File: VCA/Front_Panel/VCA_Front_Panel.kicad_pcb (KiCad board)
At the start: 2 copper layers, 30 x 128.5 mm, 3 parts

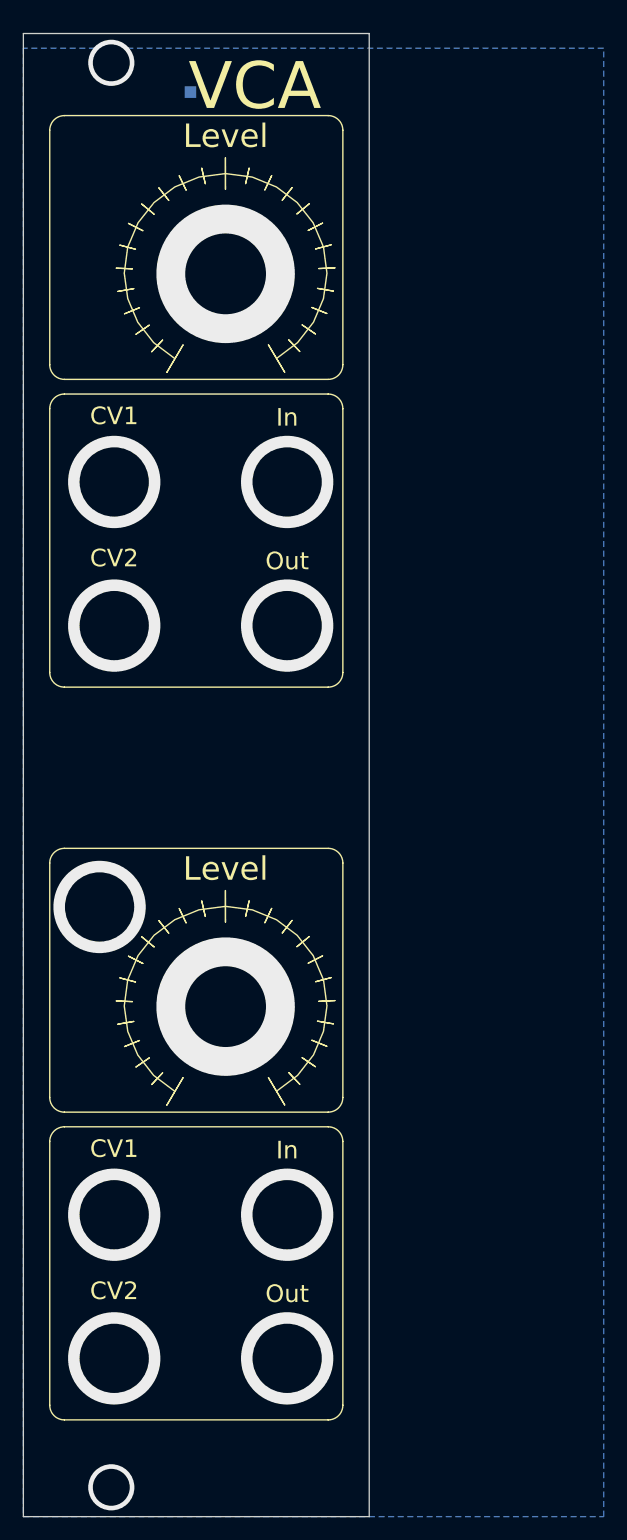
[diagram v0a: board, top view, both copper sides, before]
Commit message: Update front panel to match IO board
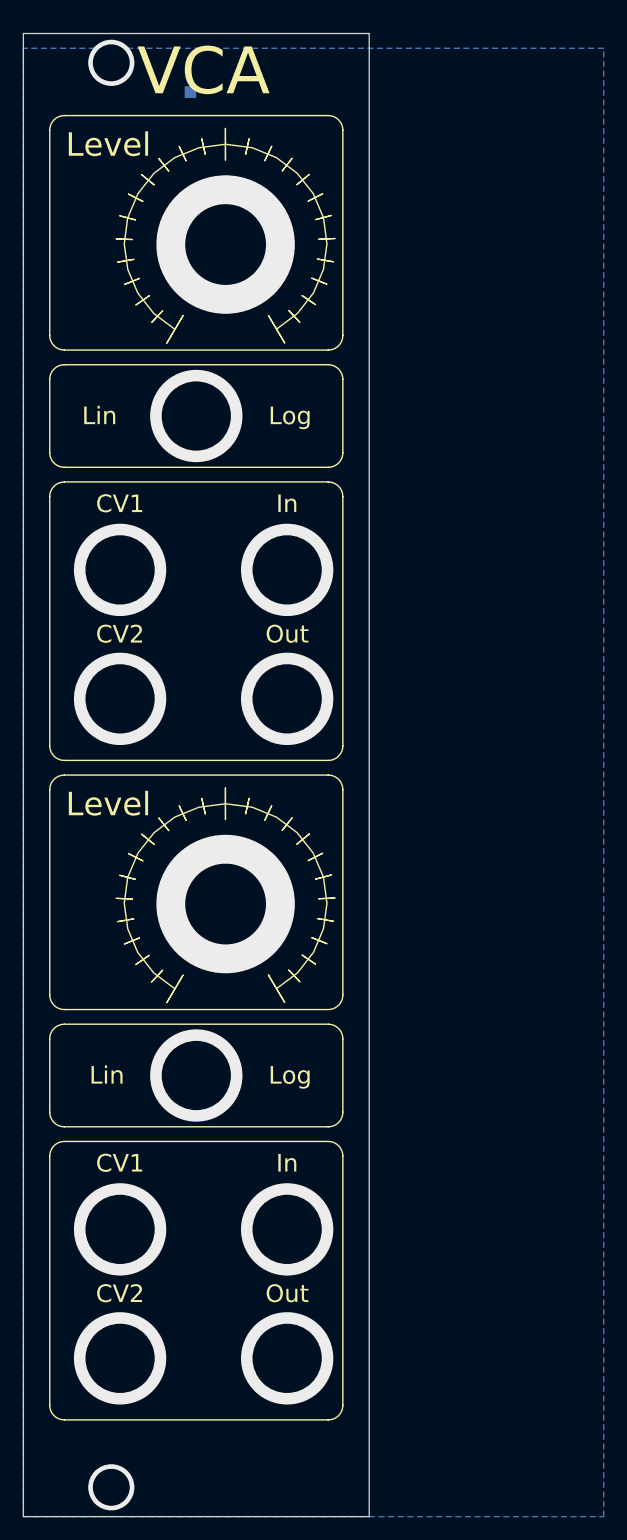
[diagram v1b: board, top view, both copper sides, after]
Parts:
- moved tick_marks 8.89 mm to (81.3, 114.6)
- moved tick_marks 2.54 mm to (81.3, 57.4)
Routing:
- net GND: vias 7 -> 14
- net (no net): vias 6 -> 0
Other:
- board text added: "Lin"
- board text added: "Log"

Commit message: Clean up VCA boards
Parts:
- added REF**: OSHW-Logo2_7.3x6mm_SilkScreen, Symbol:OSHW-Logo2_7.3x6mm_SilkScreen, B.Cu at (70.1, 51.8)
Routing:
- added copper zone on F.Cu, net GND
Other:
- board text added: "WH"

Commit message: Bunch of bug fixes and tweaks
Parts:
- removed TP1: TestPoint, TestPoint:TestPoint_Pad_1.0x1.0mm
- added H1: Level_A, Eurorack:pot_fp_hole, F.Cu at (81.3, 58.2)
- added H10: In_B, Eurorack:jack_fp_hole, F.Cu at (86.6, 143.5)
- added H11: Out_A, Eurorack:jack_fp_hole, F.Cu at (86.6, 97.5)
- added H12: Out_B, Eurorack:jack_fp_hole, F.Cu at (86.6, 154.7)
- added H13: Top_MH, Eurorack:eurorack_mounting_hole, F.Cu at (71.4, 42.9)
- added H14: Bottom_MH, Eurorack:eurorack_mounting_hole, F.Cu at (71.4, 165.4)
- added H2: Level_B, Eurorack:pot_fp_hole, F.Cu at (81.3, 115.3)
- added H3: Lin_Log_A, Eurorack:jack_fp_hole, F.Cu at (78.7, 73.0)
- added H4: Lin_Log_B, Eurorack:jack_fp_hole, F.Cu at (78.7, 130.2)
- added H5: CV1_A, Eurorack:jack_fp_hole, F.Cu at (72.1, 86.4)
- added H6: CV1_B, Eurorack:jack_fp_hole, F.Cu at (72.1, 143.5)
- added H7: CV2_A, Eurorack:jack_fp_hole, F.Cu at (72.1, 97.5)
- added H8: CV2_B, Eurorack:jack_fp_hole, F.Cu at (72.1, 154.7)
- added H9: In_A, Eurorack:jack_fp_hole, F.Cu at (86.6, 86.4)
- moved REF** 13.5 mm to (81.5, 44.6)
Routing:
- net GND: vias 14 -> 0
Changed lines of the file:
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@@
-(kicad_pcb (version 20171130) (host pcbnew 5.1.4)
+(kicad_pcb (version 20171130) (host pcbnew "(5.1.4-0-10_14)")
   (general
     (thickness 1.6)
     (drawings 69)
-    (tracks 14)
+    (tracks 0)
     (zones 0)
-    (modules 4)
+    (modules 17)
     (nets 2)
   )
@@
       (outputformat 1)
       (mirror false)
-      (drillshape 1)
+      (drillshape 0)
       (scaleselection 1)
-      (outputdirectory ""))
+      (outputdirectory "Gerbers/"))
   )
   (net 0 "")
@@
   )
   (module Symbol:OSHW-Logo2_7.3x6mm_SilkScreen (layer B.Cu)
-    (at 70.104 51.816 180)
+    (at 81.534 44.577 180)
     (descr "Open Source Hardware Symbol")
     (tags "Logo Symbol OSHW")
@@
       (xy 4.437832 -6.820018) (xy 2.326012 -7.684565) (xy 0 -7.988525)) (layer F.SilkS) (width 0))
   )
-  (module TestPoint:TestPoint_Pad_1.0x1.0mm (layer B.Cu)
-    (at 78.232 44.958)
-    (descr "SMD rectangular pad as test Point, square 1.0mm side length")
-    (tags "test point SMD pad rectangle square")
-    (attr virtual)
-    (fp_text reference TP1 (at 0 1.448) (layer B.SilkS) hide
-      (effects (font (size 1 1) (thickness 0.15)) (justify mirror))
-    )
-    (fp_text value TestPoint (at 0 -1.55) (layer B.Fab) hide
-      (effects (font (size 1 1) (thickness 0.15)) (justify mirror))
-    )
-    (fp_text user %R (at 0 1.45) (layer B.Fab) hide
-      (effects (font (size 1 1) (thickness 0.15)) (justify mirror))
-    )
-    (fp_line (start -0.7 0.7) (end 0.7 0.7) (layer B.SilkS) (width 0.12))
-    (fp_line (start 0.7 0.7) (end 0.7 -0.7) (layer B.SilkS) (width 0.12))
-    (fp_line (start 0.7 -0.7) (end -0.7 -0.7) (layer B.SilkS) (width 0.12))
-    (fp_line (start -0.7 -0.7) (end -0.7 0.7) (layer B.SilkS) (width 0.12))
-    (fp_line (start -1 1) (end 1 1) (layer B.CrtYd) (width 0.05))
-    (fp_line (start -1 1) (end -1 -1) (layer B.CrtYd) (width 0.05))
-    (fp_line (start 1 -1) (end 1 1) (layer B.CrtYd) (width 0.05))
-    (fp_line (start 1 -1) (end -1 -1) (layer B.CrtYd) (width 0.05))
-    (pad 1 smd rect (at 0 0) (size 1 1) (layers B.Cu B.Mask)
+  (module Eurorack:pot_fp_hole (layer F.Cu)
+    (at 81.28 58.166)
+    (fp_text reference H1 (at 0 0.5) (layer F.SilkS) hide
+      (effects (font (size 1 1) (thickness 0.15)))
+    )
+    (fp_text value Level_A (at 0 -0.5) (layer F.Fab) hide
+      (effects (font (size 1 1) (thickness 0.15)))
+    )
+    (pad 1 thru_hole circle (at 0 0) (size 11.999999 11.999999) (drill 7.300011) (layers *.Cu *.Mask)
+      (net 1 GND))
+  )
+  (module Eurorack:pot_fp_hole (layer F.Cu)
+    (at 81.28 115.316)
+    (fp_text reference H2 (at 0 0.5) (layer F.SilkS) hide
+      (effects (font (size 1 1) (thickness 0.15)))
+    )
+    (fp_text value Level_B (at 0 -0.5) (layer F.Fab) hide
+      (effects (font (size 1 1) (thickness 0.15)))
+    )
+    (pad 1 thru_hole circle (at 0 0) (size 11.999999 11.999999) (drill 7.300011) (layers *.Cu *.Mask)
+      (net 1 GND))
+  )
+  (module Eurorack:jack_fp_hole (layer F.Cu)
+    (at 78.74 73.025)
+    (fp_text reference H3 (at 0 0.5) (layer F.SilkS) hide
+      (effects (font (size 1 1) (thickness 0.15)))
+    )
+    (fp_text value Lin_Log_A (at 0 -0.5) (layer F.Fab) hide
+      (effects (font (size 1 1) (thickness 0.15)))
+    )
+    (pad 1 thru_hole circle (at 0 0) (size 7.999999 7.999999) (drill 6.199988) (layers *.Cu *.Mask)
+      (net 1 GND))
+  )
+  (module Eurorack:jack_fp_hole (layer F.Cu)
+    (at 78.74 130.175)
+    (fp_text reference H4 (at 0 0.5) (layer F.SilkS) hide
+      (effects (font (size 1 1) (thickness 0.15)))
+    )
+    (fp_text value Lin_Log_B (at 0 -0.5) (layer F.Fab) hide
+      (effects (font (size 1 1) (thickness 0.15)))
+    )
+    (pad 1 thru_hole circle (at 0 0) (size 7.999999 7.999999) (drill 6.199988) (layers *.Cu *.Mask)
+      (net 1 GND))
+  )
+  (module Eurorack:jack_fp_hole (layer F.Cu)
+    (at 72.136 86.36)
+    (fp_text reference H5 (at 0 0.5) (layer F.SilkS) hide
+      (effects (font (size 1 1) (thickness 0.15)))
+    )
+    (fp_text value CV1_A (at 0 -0.5) (layer F.Fab) hide
+      (effects (font (size 1 1) (thickness 0.15)))
+    )
+    (pad 1 thru_hole circle (at 0 0) (size 7.999999 7.999999) (drill 6.199988) (layers *.Cu *.Mask)
+      (net 1 GND))
+  )
+  (module Eurorack:jack_fp_hole (layer F.Cu)
+    (at 72.136 143.51)
+    (fp_text reference H6 (at 0 0.5) (layer F.SilkS) hide
+      (effects (font (size 1 1) (thickness 0.15)))
+    )
+    (fp_text value CV1_B (at 0 -0.5) (layer F.Fab) hide
+      (effects (font (size 1 1) (thickness 0.15)))
+    )
+    (pad 1 thru_hole circle (at 0 0) (size 7.999999 7.999999) (drill 6.199988) (layers *.Cu *.Mask)
+      (net 1 GND))
+  )
+  (module Eurorack:jack_fp_hole (layer F.Cu)
+    (at 72.136 97.536)
+    (fp_text reference H7 (at 0 0.5) (layer F.SilkS) hide
+      (effects (font (size 1 1) (thickness 0.15)))
+    )
+    (fp_text value CV2_A (at 0 -0.5) (layer F.Fab) hide
+      (effects (font (size 1 1) (thickness 0.15)))
+    )
+    (pad 1 thru_hole circle (at 0 0) (size 7.999999 7.999999) (drill 6.199988) (layers *.Cu *.Mask)
+      (net 1 GND))
+  )
+  (module Eurorack:jack_fp_hole (layer F.Cu)
+    (at 72.136 154.686)
+    (fp_text reference H8 (at 0 0.5) (layer F.SilkS) hide
+      (effects (font (size 1 1) (thickness 0.15)))
+    )
+    (fp_text value CV2_B (at 0 -0.5) (layer F.Fab) hide
+      (effects (font (size 1 1) (thickness 0.15)))
+    )
+    (pad 1 thru_hole circle (at 0 0) (size 7.999999 7.999999) (drill 6.199988) (layers *.Cu *.Mask)
+      (net 1 GND))
+  )
+  (module Eurorack:jack_fp_hole (layer F.Cu)
+    (at 86.614 86.36)
+    (fp_text reference H9 (at 0 0.5) (layer F.SilkS) hide
+      (effects (font (size 1 1) (thickness 0.15)))
+    )
+    (fp_text value In_A (at 0 -0.5) (layer F.Fab) hide
+      (effects (font (size 1 1) (thickness 0.15)))
+    )
+    (pad 1 thru_hole circle (at 0 0) (size 7.999999 7.999999) (drill 6.199988) (layers *.Cu *.Mask)
+      (net 1 GND))
+  )
+  (module Eurorack:jack_fp_hole (layer F.Cu)
+    (at 86.614 143.51)
+    (fp_text reference H10 (at 0 0.5) (layer F.SilkS) hide
+      (effects (font (size 1 1) (thickness 0.15)))
+    )
+    (fp_text value In_B (at 0 -0.5) (layer F.Fab) hide
+      (effects (font (size 1 1) (thickness 0.15)))
+    )
+    (pad 1 thru_hole circle (at 0 0) (size 7.999999 7.999999) (drill 6.199988) (layers *.Cu *.Mask)
+      (net 1 GND))
+  )
+  (module Eurorack:jack_fp_hole (layer F.Cu)
+    (at 86.614 97.536)
+    (fp_text reference H11 (at 0 0.5) (layer F.SilkS) hide
+      (effects (font (size 1 1) (thickness 0.15)))
+    )
+    (fp_text value Out_A (at 0 -0.5) (layer F.Fab) hide
+      (effects (font (size 1 1) (thickness 0.15)))
+    )
+    (pad 1 thru_hole circle (at 0 0) (size 7.999999 7.999999) (drill 6.199988) (layers *.Cu *.Mask)
+      (net 1 GND))
+  )
+  (module Eurorack:jack_fp_hole (layer F.Cu)
+    (at 86.614 154.686)
+    (fp_text reference H12 (at 0 0.5) (layer F.SilkS) hide
+      (effects (font (size 1 1) (thickness 0.15)))
+    )
+    (fp_text value Out_B (at 0 -0.5) (layer F.Fab) hide
+      (effects (font (size 1 1) (thickness 0.15)))
+    )
+    (pad 1 thru_hole circle (at 0 0) (size 7.999999 7.999999) (drill 6.199988) (layers *.Cu *.Mask)
+      (net 1 GND))
+  )
+  (module Eurorack:eurorack_mounting_hole (layer F.Cu)
+    (at 71.374 42.926)
+    (fp_text reference H13 (at 0 0.5) (layer F.SilkS) hide
+      (effects (font (size 1 1) (thickness 0.15)))
+    )
+    (fp_text value Top_MH (at 0 -0.5) (layer F.Fab) hide
+      (effects (font (size 1 1) (thickness 0.15)))
+    )
+    (pad 1 thru_hole circle (at 0 0) (size 5 5) (drill 3.2) (layers *.Cu *.Mask)
+      (net 1 GND))
+  )
+  (module Eurorack:eurorack_mounting_hole (layer F.Cu)
+    (at 71.374 165.354)
+    (fp_text reference H14 (at 0 0.5) (layer F.SilkS) hide
+      (effects (font (size 1 1) (thickness 0.15)))
+    )
+    (fp_text value Bottom_MH (at 0 -0.5) (layer F.Fab) hide
+      (effects (font (size 1 1) (thickness 0.15)))
+    )
+    (pad 1 thru_hole circle (at 0 0) (size 5 5) (drill 3.2) (layers *.Cu *.Mask)
       (net 1 GND))
   )
@@
   (gr_line (start 93.726 39.878) (end 93.726 168.402) (layer Edge.Cuts) (width 0.05))
   (gr_line (start 63.754 39.878) (end 93.726 39.878) (layer Edge.Cuts) (width 0.05))
-  (via (at 78.74 73.025) (size 7.999999) (drill 6.199988) (layers F.Cu B.Cu) (net 1))
-  (via (at 81.28 58.166) (size 11.999999) (drill 7.300011) (layers F.Cu B.Cu) (net 1))
-  (via (at 86.614 97.536) (size 7.999999) (drill 6.199988) (layers F.Cu B.Cu) (net 1))
-  (via (at 72.136 86.36) (size 7.999999) (drill 6.199988) (layers F.Cu B.Cu) (net 1))
-  (via (at 72.136 97.536) (size 7.999999) (drill 6.199988) (layers F.Cu B.Cu) (net 1))
-  (via (at 86.614 86.36) (size 7.999999) (drill 6.199988) (layers F.Cu B.Cu) (net 1))
-  (via (at 78.74 130.175) (size 7.999999) (drill 6.199988) (layers F.Cu B.Cu) (net 1))
-  (via (at 86.614 143.51) (size 7.999999) (drill 6.199988) (layers F.Cu B.Cu) (net 1))
-  (via (at 81.28 115.316) (size 11.999999) (drill 7.300011) (layers F.Cu B.Cu) (net 1))
-  (via (at 86.614 154.686) (size 7.999999) (drill 6.199988) (layers F.Cu B.Cu) (net 1))
-  (via (at 72.136 143.51) (size 7.999999) (drill 6.199988) (layers F.Cu B.Cu) (net 1))
-  (via (at 72.136 154.686) (size 7.999999) (drill 6.199988) (layers F.Cu B.Cu) (net 1))
-  (via (at 71.374 42.926) (size 4.99999) (drill 3.2004) (layers F.Cu B.Cu) (net 1))
-  (via (at 71.374 165.354) (size 4.99999) (drill 3.2004) (layers F.Cu B.Cu) (net 1))
   (zone (net 1) (net_name GND) (layer F.Cu) (hatch edge 0.508)
-    (connect_pads (clearance 0.508))
+    (connect_pads yes (clearance 0.508))
     (min_thickness 0.254)
     (fill yes (arc_segments 32) (thermal_gap 0.508) (thermal_bridge_width 0.508))
@@
   )
   (zone (net 1) (net_name GND) (layer B.Cu) (hatch edge 0.508)
-    (connect_pads (clearance 0.508))
+    (connect_pads yes (clearance 0.508))
     (min_thickness 0.254)
     (fill yes (arc_segments 32) (thermal_gap 0.508) (thermal_bridge_width 0.508))

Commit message: Clean up layout of VCA board
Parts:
- tick_marks (x2): footprint AS3340_VCO_FP:knob_tick_marks -> Eurorack:knob_tick_marks
